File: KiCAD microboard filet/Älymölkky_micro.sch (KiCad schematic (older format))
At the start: 32 parts, among them U1 nRF52810-QCxx, X1 32MHz Crystal, X1_C1 12pF, X1_C2 12pF, X2 32.768 kHz Crystal, X2_C11 12pF, X2_C12 12pF

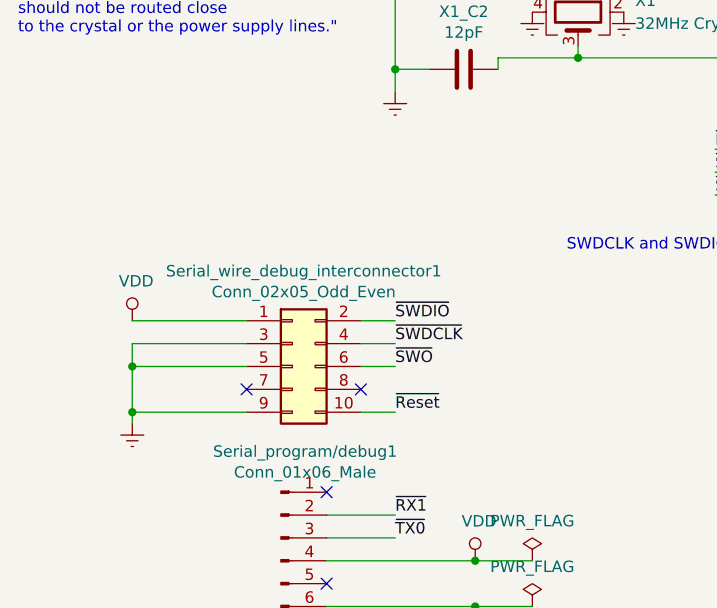
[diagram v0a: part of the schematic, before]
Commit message: Changed programming interface to standalone pinheaders
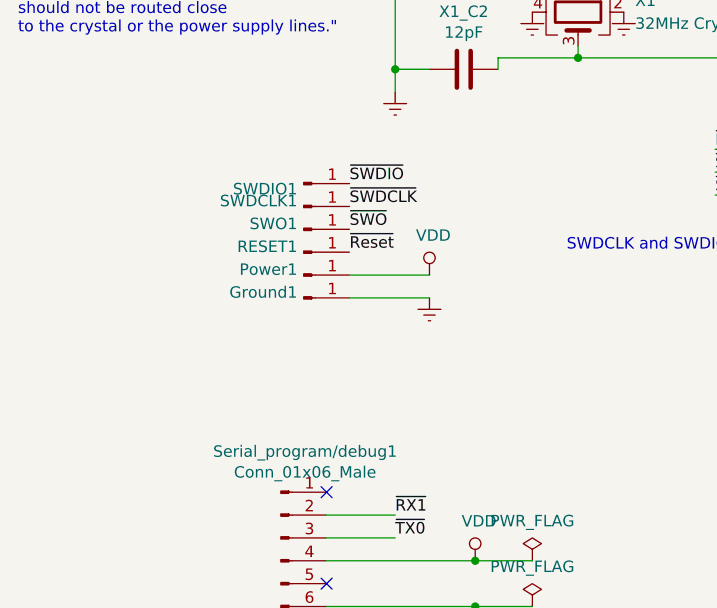
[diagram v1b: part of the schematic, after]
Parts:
- removed Serial_wire_debug_interconnector1: Conn_02x05_Odd_Even, Connector_PinHeader_1.27mm:PinHeader_2x05_P1.27mm_Vertical_SMD, symbol Connector_Generic:Conn_02x05_Odd_Even
- added Ground1, Power1, RESET1, SWDCLK1, SWDIO1, SWO1: Conn_01x01_Male, Connector_PinHeader_2.54mm:PinHeader_1x01_P2.54mm_Vertical, symbol Connector:Conn_01x01_Male
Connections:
- net Earth: now also Ground1.1 (Pin_1)
- net VDD: now also Power1.1 (Pin_1)
- net ~Reset: now also RESET1.1 (Pin_1)
- net ~SWDCLK: now also SWDCLK1.1 (Pin_1)
- net ~SWDIO: now also SWDIO1.1 (Pin_1)
- net ~SWO: now also SWO1.1 (Pin_1)
- no-connect marks 9 -> 7
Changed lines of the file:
@@
 Wire Wire Line
 	9200 1500 9300 1500
-$Comp
-L Connector_Generic:Conn_02x05_Odd_Even Serial_wire_debug_interconnector1
-U 1 1 5C65B530
-P 1750 6600
-F 0 "Serial_wire_debug_interconnector1" H 1800 7017 50  0000 C CNN
-F 1 "Conn_02x05_Odd_Even" H 1800 6926 50  0000 C CNN
-F 2 "Connector_PinHeader_1.27mm:PinHeader_2x05_P1.27mm_Vertical_SMD" H 1750 6600 50  0001 C CNN
-F 3 "~" H 1750 6600 50  0001 C CNN
-	1    1750 6600
-	1    0    0    -1
-$EndComp
 Text Notes 1700 1000 0    50   ~ 0
 Power and ground test points
@@
 Wire Wire Line
 	1700 1400 1900 1400
-Text Label 2200 6400 0    50   ~ 0
+Text Label 2000 5800 0    50   ~ 0
 ~SWDIO
-Text Label 2200 6500 0    50   ~ 0
+Text Label 2000 5900 0    50   ~ 0
 ~SWDCLK
-Text Label 2200 6800 0    50   ~ 0
+Text Label 2000 6100 0    50   ~ 0
 ~Reset
-NoConn ~ 2050 6700
 Text Label 5950 5550 0    50   ~ 0
 ~SWO
-Text Label 2200 6600 0    50   ~ 0
+Text Label 2000 6000 0    50   ~ 0
 ~SWO
-Wire Wire Line
-	2200 6400 2050 6400
-Wire Wire Line
-	2050 6500 2200 6500
-Wire Wire Line
-	2200 6600 2050 6600
-Wire Wire Line
-	2200 6800 2050 6800
 $Comp
 L power:VDD #PWR0115
 U 1 1 5C695765
-P 1050 6400
-F 0 "#PWR0115" H 1050 6250 50  0001 C CNN
-F 1 "VDD" H 1067 6573 50  0000 C CNN
-F 2 "" H 1050 6400 50  0001 C CNN
-F 3 "" H 1050 6400 50  0001 C CNN
-	1    1050 6400
+P 2350 6200
+F 0 "#PWR0115" H 2350 6050 50  0001 C CNN
+F 1 "VDD" H 2367 6373 50  0000 C CNN
+F 2 "" H 2350 6200 50  0001 C CNN
+F 3 "" H 2350 6200 50  0001 C CNN
+	1    2350 6200
 	1    0    0    -1
 $EndComp
@@
 L power:Earth #PWR0116
 U 1 1 5C6957BC
-P 1050 6850
-F 0 "#PWR0116" H 1050 6600 50  0001 C CNN
-F 1 "Earth" H 1050 6700 50  0001 C CNN
-F 2 "" H 1050 6850 50  0001 C CNN
-F 3 "~" H 1050 6850 50  0001 C CNN
-	1    1050 6850
-	1    0    0    -1
-$EndComp
-Wire Wire Line
-	1050 6400 1550 6400
-Wire Wire Line
-	1550 6500 1050 6500
-Wire Wire Line
-	1050 6500 1050 6600
-Wire Wire Line
-	1050 6600 1550 6600
-Wire Wire Line
-	1550 6800 1050 6800
-Wire Wire Line
-	1050 6800 1050 6600
-Connection ~ 1050 6600
-Wire Wire Line
-	1050 6800 1050 6850
-Connection ~ 1050 6800
-NoConn ~ 1550 6700
+P 2350 6300
+F 0 "#PWR0116" H 2350 6050 50  0001 C CNN
+F 1 "Earth" H 2350 6150 50  0001 C CNN
+F 2 "" H 2350 6300 50  0001 C CNN
+F 3 "~" H 2350 6300 50  0001 C CNN
+	1    2350 6300
+	1    0    0    -1
+$EndComp
 $Comp
 L Connector:Conn_01x06_Male Serial_program/debug1
@@
 	5550 2800 5550 3400
 $Comp
-L power:Earth #PWR?
+L power:Earth #PWR0127
 U 1 1 5C8923A6
 P 5800 3200
-F 0 "#PWR?" H 5800 2950 50  0001 C CNN
+F 0 "#PWR0127" H 5800 2950 50  0001 C CNN
 F 1 "Earth" H 5800 3050 50  0001 C CNN
 F 2 "" H 5800 3200 50  0001 C CNN
@@
 $EndComp
 $Comp
-L power:Earth #PWR?
+L power:Earth #PWR0128
 U 1 1 5C89245B
 P 6400 3200
-F 0 "#PWR?" H 6400 2950 50  0001 C CNN
+F 0 "#PWR0128" H 6400 2950 50  0001 C CNN
 F 1 "Earth" H 6400 3050 50  0001 C CNN
 F 2 "" H 6400 3200 50  0001 C CNN
@@
 Wire Wire Line
 	5800 3150 5800 3200
+$Comp
+L Connector:Conn_01x01_Male SWDIO1
+U 1 1 5C8807BA
+P 1800 5800
+F 0 "SWDIO1" H 1772 5776 50  0000 R CNN
+F 1 "Conn_01x01_Male" H 1773 5821 50  0001 R CNN
+F 2 "Connector_PinHeader_2.54mm:PinHeader_1x01_P2.54mm_Vertical" H 1800 5800 50  0001 C CNN
+F 3 "~" H 1800 5800 50  0001 C CNN
+	1    1800 5800
+	1    0    0    -1
+$EndComp
+$Comp
+L Connector:Conn_01x01_Male SWDCLK1
+U 1 1 5C880E14
+P 1800 5900
+F 0 "SWDCLK1" H 1772 5876 50  0000 R CNN
+F 1 "Conn_01x01_Male" H 1773 5921 50  0001 R CNN
+F 2 "Connector_PinHeader_2.54mm:PinHeader_1x01_P2.54mm_Vertical" H 1800 5900 50  0001 C CNN
+F 3 "~" H 1800 5900 50  0001 C CNN
+	1    1800 5900
+	1    0    0    1
+$EndComp
+$Comp
+L Connector:Conn_01x01_Male SWO1
+U 1 1 5C8817A7
+P 1800 6000
+F 0 "SWO1" H 1772 5976 50  0000 R CNN
+F 1 "Conn_01x01_Male" H 1773 6021 50  0001 R CNN
+F 2 "Connector_PinHeader_2.54mm:PinHeader_1x01_P2.54mm_Vertical" H 1800 6000 50  0001 C CNN
+F 3 "~" H 1800 6000 50  0001 C CNN
+	1    1800 6000
+	1    0    0    1
+$EndComp
+$Comp
+L Connector:Conn_01x01_Male RESET1
+U 1 1 5C881848
+P 1800 6100
+F 0 "RESET1" H 1772 6076 50  0000 R CNN
+F 1 "Conn_01x01_Male" H 1773 6121 50  0001 R CNN
+F 2 "Connector_PinHeader_2.54mm:PinHeader_1x01_P2.54mm_Vertical" H 1800 6100 50  0001 C CNN
+F 3 "~" H 1800 6100 50  0001 C CNN
+	1    1800 6100
+	1    0    0    1
+$EndComp
+$Comp
+L Connector:Conn_01x01_Male Power1
+U 1 1 5C8822A3
+P 1800 6200
+F 0 "Power1" H 1772 6176 50  0000 R CNN
+F 1 "Conn_01x01_Male" H 1773 6221 50  0001 R CNN
+F 2 "Connector_PinHeader_2.54mm:PinHeader_1x01_P2.54mm_Vertical" H 1800 6200 50  0001 C CNN
+F 3 "~" H 1800 6200 50  0001 C CNN
+	1    1800 6200
+	1    0    0    1
+$EndComp
+$Comp
+L Connector:Conn_01x01_Male Ground1
+U 1 1 5C882301
+P 1800 6300
+F 0 "Ground1" H 1772 6276 50  0000 R CNN
+F 1 "Conn_01x01_Male" H 1773 6321 50  0001 R CNN
+F 2 "Connector_PinHeader_2.54mm:PinHeader_1x01_P2.54mm_Vertical" H 1800 6300 50  0001 C CNN
+F 3 "~" H 1800 6300 50  0001 C CNN
+	1    1800 6300
+	1    0    0    1
+$EndComp
+Wire Wire Line
+	2000 6200 2350 6200
+Wire Wire Line
+	2350 6300 2000 6300
 $EndSCHEMATC

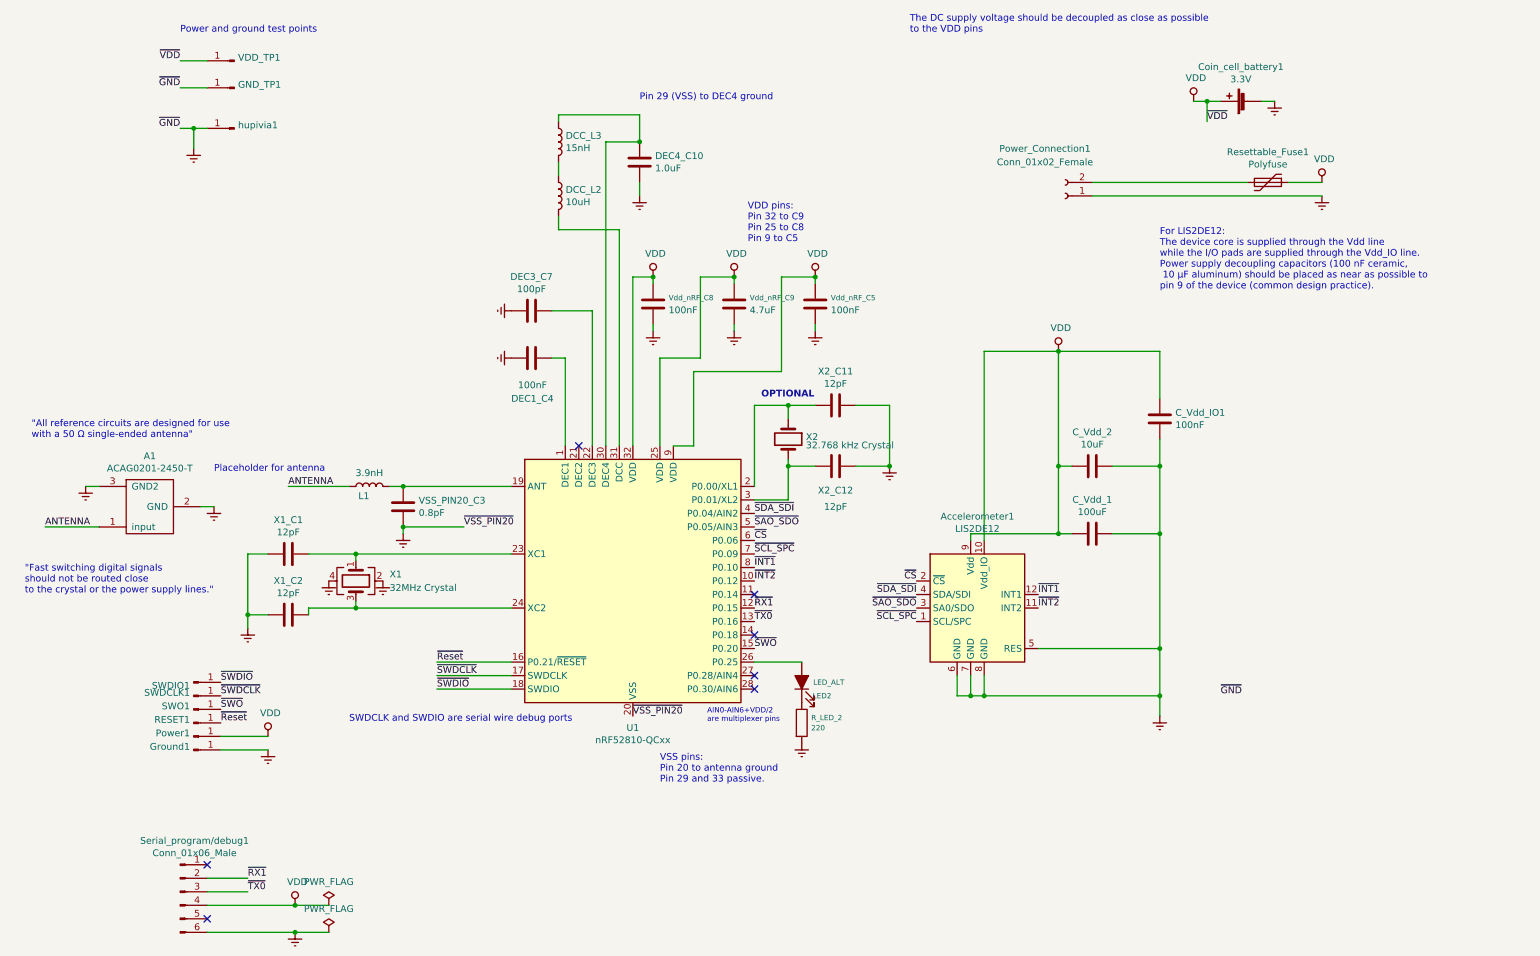
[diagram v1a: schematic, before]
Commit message: Changed serial programming pin locations and order, reorganized whole board
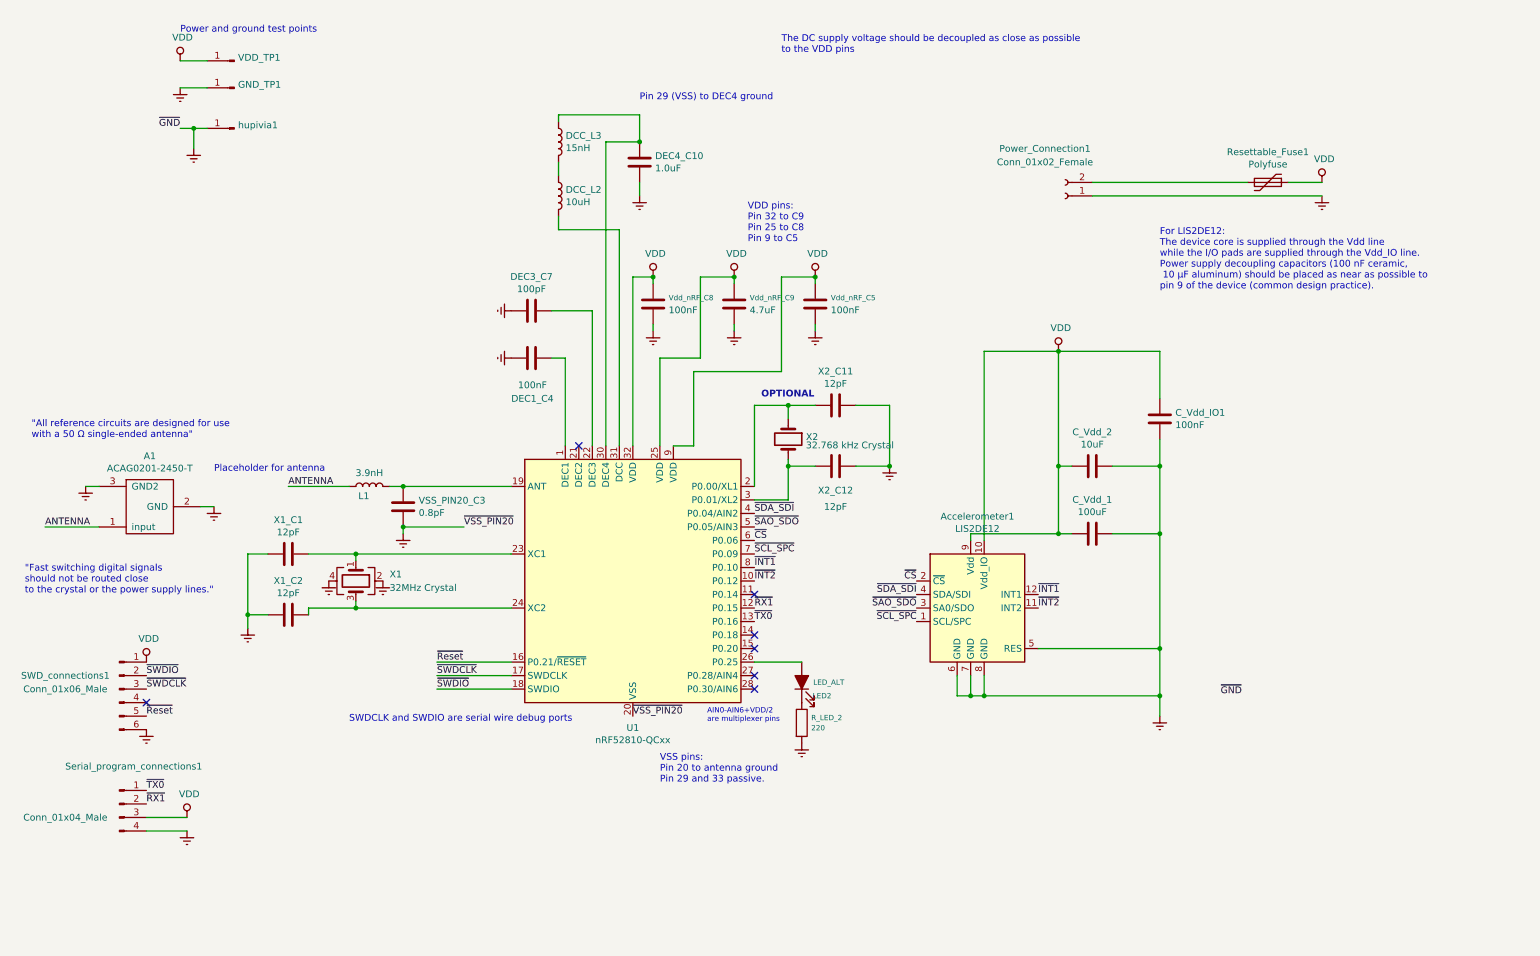
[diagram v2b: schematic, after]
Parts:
- removed Coin_cell_battery1: 3.3V, symbol Device:Battery_Cell
- removed Ground1, Power1, RESET1, SWDCLK1, SWDIO1, SWO1: Conn_01x01_Male, Connector_PinHeader_2.54mm:PinHeader_1x01_P2.54mm_Vertical, symbol Connector:Conn_01x01_Male
- removed Serial_program/debug1: Conn_01x06_Male, Connector_PinHeader_2.54mm:PinHeader_1x06_P2.54mm_Vertical, symbol Connector:Conn_01x06_Male
- added SWD_connections1: Conn_01x06_Male, Connector_PinHeader_2.54mm:PinHeader_1x06_P2.54mm_Vertical, symbol Connector:Conn_01x06_Male
- added Serial_program_connections1: Conn_01x04_Male, Connector_PinHeader_2.54mm:PinHeader_1x04_P2.54mm_Vertical, symbol Connector:Conn_01x04_Male
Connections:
- net Earth: now also SWD_connections1.6 (Pin_6), Serial_program_connections1.4 (Pin_4)
- net VDD: now also SWD_connections1.1 (Pin_1), Serial_program_connections1.3 (Pin_3)
- net ~RX1: now also Serial_program_connections1.2 (Pin_2)
- net ~Reset: now also SWD_connections1.5 (Pin_5)
- net ~SWDCLK: now also SWD_connections1.3 (Pin_3)
- net ~SWDIO: now also SWD_connections1.2 (Pin_2)
- net ~TX0: now also Serial_program_connections1.1 (Pin_1)
- net ~SWO: no longer names the net of U1.15 (P0.20)
